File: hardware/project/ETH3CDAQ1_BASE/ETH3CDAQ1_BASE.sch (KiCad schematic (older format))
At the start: 0 parts

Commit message: Schematic design
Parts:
- added H101, H102: MountingHole, MountingHole:MountingHole_2.7mm_M2.5_DIN965_Pad, symbol Mechanical:MountingHole
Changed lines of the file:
@@
 F1 "Channel3.sch" 50
 $EndSheet
+$Comp
+L Mechanical:MountingHole H101
+U 1 1 5FD1DE86
+P 1500 7000
+F 0 "H101" H 1600 7046 50  0000 L CNN
+F 1 "MountingHole" H 1600 6955 50  0000 L CNN
+F 2 "MountingHole:MountingHole_2.7mm_M2.5_DIN965_Pad" H 1500 7000 50  0001 C CNN
+F 3 "~" H 1500 7000 50  0001 C CNN
+	1    1500 7000
+	1    0    0    -1
+$EndComp
+$Comp
+L Mechanical:MountingHole H102
+U 1 1 5FD1EC9A
+P 2350 7000
+F 0 "H102" H 2450 7046 50  0000 L CNN
+F 1 "MountingHole" H 2450 6955 50  0000 L CNN
+F 2 "MountingHole:MountingHole_2.7mm_M2.5_DIN965_Pad" H 2350 7000 50  0001 C CNN
+F 3 "~" H 2350 7000 50  0001 C CNN
+	1    2350 7000
+	1    0    0    -1
+$EndComp
 $EndSCHEMATC

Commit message: PCB layout.
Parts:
- added H103, H104, H105, H106, H107, H108: MountingHole, MountingHole:MountingHole_2.7mm_M2.5_DIN965_Pad, symbol Mechanical:MountingHole
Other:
- moved on the sheet: H101, H102
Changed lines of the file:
@@
 L Mechanical:MountingHole H101
 U 1 1 5FD1DE86
-P 1500 7000
-F 0 "H101" H 1600 7046 50  0000 L CNN
-F 1 "MountingHole" H 1600 6955 50  0000 L CNN
-F 2 "MountingHole:MountingHole_2.7mm_M2.5_DIN965_Pad" H 1500 7000 50  0001 C CNN
-F 3 "~" H 1500 7000 50  0001 C CNN
-	1    1500 7000
+P 900 6700
+F 0 "H101" H 1000 6746 50  0000 L CNN
+F 1 "MountingHole" H 1000 6655 50  0000 L CNN
+F 2 "MountingHole:MountingHole_2.7mm_M2.5_DIN965_Pad" H 900 6700 50  0001 C CNN
+F 3 "~" H 900 6700 50  0001 C CNN
+	1    900  6700
 	1    0    0    -1
 $EndComp
@@
 L Mechanical:MountingHole H102
 U 1 1 5FD1EC9A
-P 2350 7000
-F 0 "H102" H 2450 7046 50  0000 L CNN
-F 1 "MountingHole" H 2450 6955 50  0000 L CNN
-F 2 "MountingHole:MountingHole_2.7mm_M2.5_DIN965_Pad" H 2350 7000 50  0001 C CNN
-F 3 "~" H 2350 7000 50  0001 C CNN
-	1    2350 7000
+P 1750 6700
+F 0 "H102" H 1850 6746 50  0000 L CNN
+F 1 "MountingHole" H 1850 6655 50  0000 L CNN
+F 2 "MountingHole:MountingHole_2.7mm_M2.5_DIN965_Pad" H 1750 6700 50  0001 C CNN
+F 3 "~" H 1750 6700 50  0001 C CNN
+	1    1750 6700
 	1    0    0    -1
 $EndComp
+$Comp
+L Mechanical:MountingHole H105
+U 1 1 5FB9C26E
+P 900 7450
+F 0 "H105" H 1000 7496 50  0000 L CNN
+F 1 "MountingHole" H 1000 7405 50  0000 L CNN
+F 2 "MountingHole:MountingHole_2.7mm_M2.5_DIN965_Pad" H 900 7450 50  0001 C CNN
+F 3 "~" H 900 7450 50  0001 C CNN
+	1    900  7450
+	1    0    0    -1
+$EndComp
+$Comp
+L Mechanical:MountingHole H108
+U 1 1 5FB9C274
+P 1750 7450
+F 0 "H108" H 1850 7496 50  0000 L CNN
+F 1 "MountingHole" H 1850 7405 50  0000 L CNN
+F 2 "MountingHole:MountingHole_2.7mm_M2.5_DIN965_Pad" H 1750 7450 50  0001 C CNN
+F 3 "~" H 1750 7450 50  0001 C CNN
+	1    1750 7450
+	1    0    0    -1
+$EndComp
+$Comp
+L Mechanical:MountingHole H104
+U 1 1 5FB9C81C
+P 900 7200
+F 0 "H104" H 1000 7246 50  0000 L CNN
+F 1 "MountingHole" H 1000 7155 50  0000 L CNN
+F 2 "MountingHole:MountingHole_2.7mm_M2.5_DIN965_Pad" H 900 7200 50  0001 C CNN
+F 3 "~" H 900 7200 50  0001 C CNN
+	1    900  7200
+	1    0    0    -1
+$EndComp
+$Comp
+L Mechanical:MountingHole H107
+U 1 1 5FB9C822
+P 1750 7200
+F 0 "H107" H 1850 7246 50  0000 L CNN
+F 1 "MountingHole" H 1850 7155 50  0000 L CNN
+F 2 "MountingHole:MountingHole_2.7mm_M2.5_DIN965_Pad" H 1750 7200 50  0001 C CNN
+F 3 "~" H 1750 7200 50  0001 C CNN
+	1    1750 7200
+	1    0    0    -1
+$EndComp
+$Comp
+L Mechanical:MountingHole H103
+U 1 1 5FB9CAB2
+P 900 6950
+F 0 "H103" H 1000 6996 50  0000 L CNN
+F 1 "MountingHole" H 1000 6905 50  0000 L CNN
+F 2 "MountingHole:MountingHole_2.7mm_M2.5_DIN965_Pad" H 900 6950 50  0001 C CNN
+F 3 "~" H 900 6950 50  0001 C CNN
+	1    900  6950
+	1    0    0    -1
+$EndComp
+$Comp
+L Mechanical:MountingHole H106
+U 1 1 5FB9CAB8
+P 1750 6950
+F 0 "H106" H 1850 6996 50  0000 L CNN
+F 1 "MountingHole" H 1850 6905 50  0000 L CNN
+F 2 "MountingHole:MountingHole_2.7mm_M2.5_DIN965_Pad" H 1750 6950 50  0001 C CNN
+F 3 "~" H 1750 6950 50  0001 C CNN
+	1    1750 6950
+	1    0    0    -1
+$EndComp

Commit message: PCB design
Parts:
- H101, H102: footprint MountingHole:MountingHole_2.7mm_M2.5_DIN965_Pad -> MountingHole:MountingHole_3.2mm_M3_DIN965_Pad
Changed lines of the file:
@@
 F 0 "H101" H 1000 6746 50  0000 L CNN
 F 1 "MountingHole" H 1000 6655 50  0000 L CNN
-F 2 "MountingHole:MountingHole_2.7mm_M2.5_DIN965_Pad" H 900 6700 50  0001 C CNN
+F 2 "MountingHole:MountingHole_3.2mm_M3_DIN965_Pad" H 900 6700 50  0001 C CNN
 F 3 "~" H 900 6700 50  0001 C CNN
 	1    900  6700
@@
 F 0 "H102" H 1850 6746 50  0000 L CNN
 F 1 "MountingHole" H 1850 6655 50  0000 L CNN
-F 2 "MountingHole:MountingHole_2.7mm_M2.5_DIN965_Pad" H 1750 6700 50  0001 C CNN
+F 2 "MountingHole:MountingHole_3.2mm_M3_DIN965_Pad" H 1750 6700 50  0001 C CNN
 F 3 "~" H 1750 6700 50  0001 C CNN
 	1    1750 6700

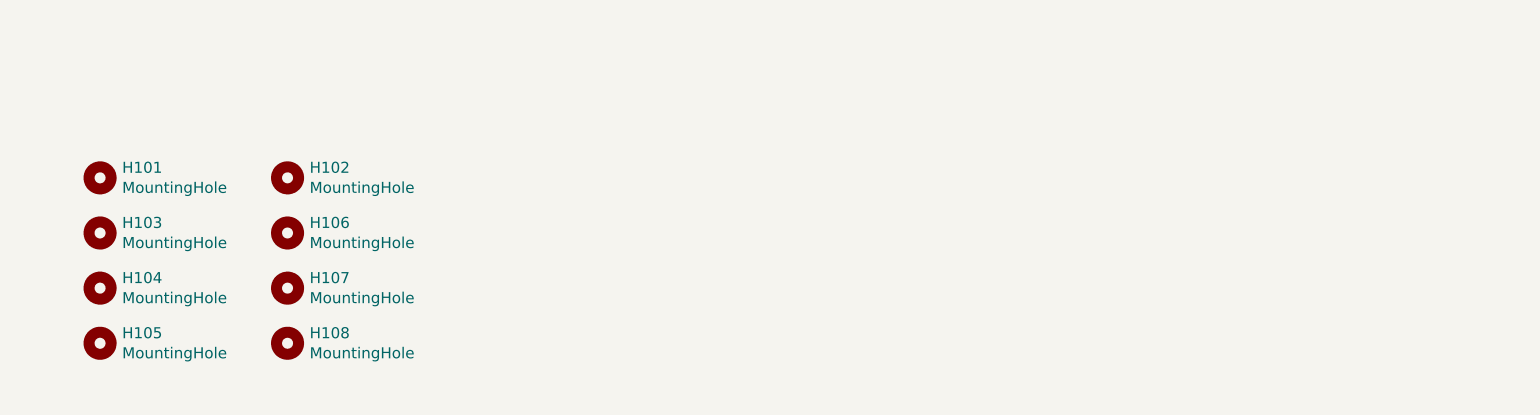
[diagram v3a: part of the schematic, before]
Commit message: Voltage front-end development
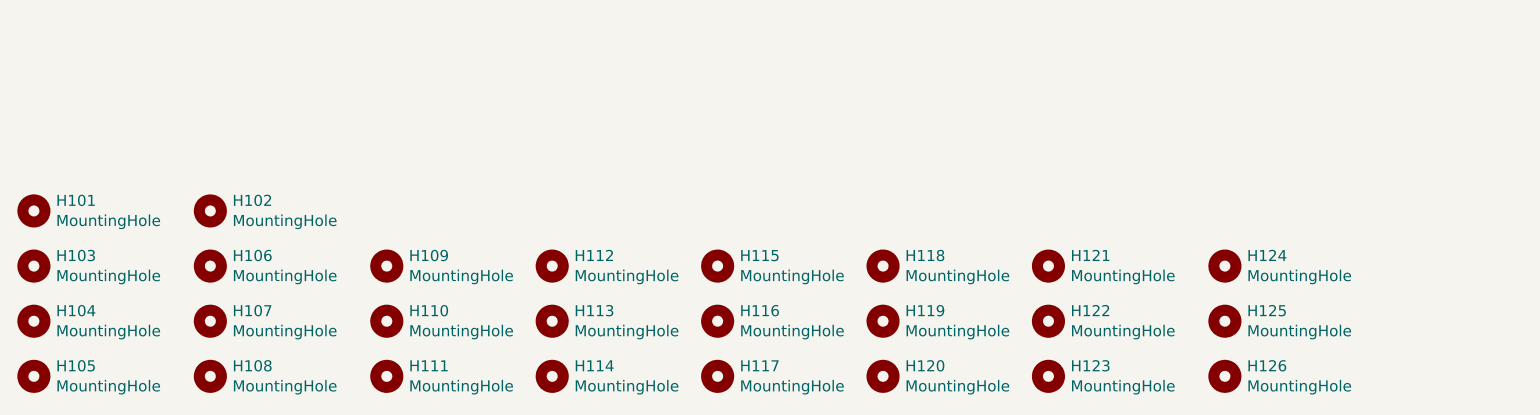
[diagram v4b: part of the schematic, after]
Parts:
- added H109, H110, H111, H112, H113, H114, H115, H116, H117, H118, H119, H120, H121, H122, H123, H124, H125, H126: MountingHole, MountingHole:MountingHole_2.7mm_M2.5_DIN965_Pad, symbol Mechanical:MountingHole
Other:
- moved on the sheet: H101, H102, H103, H104, H105, H106, H107, H108

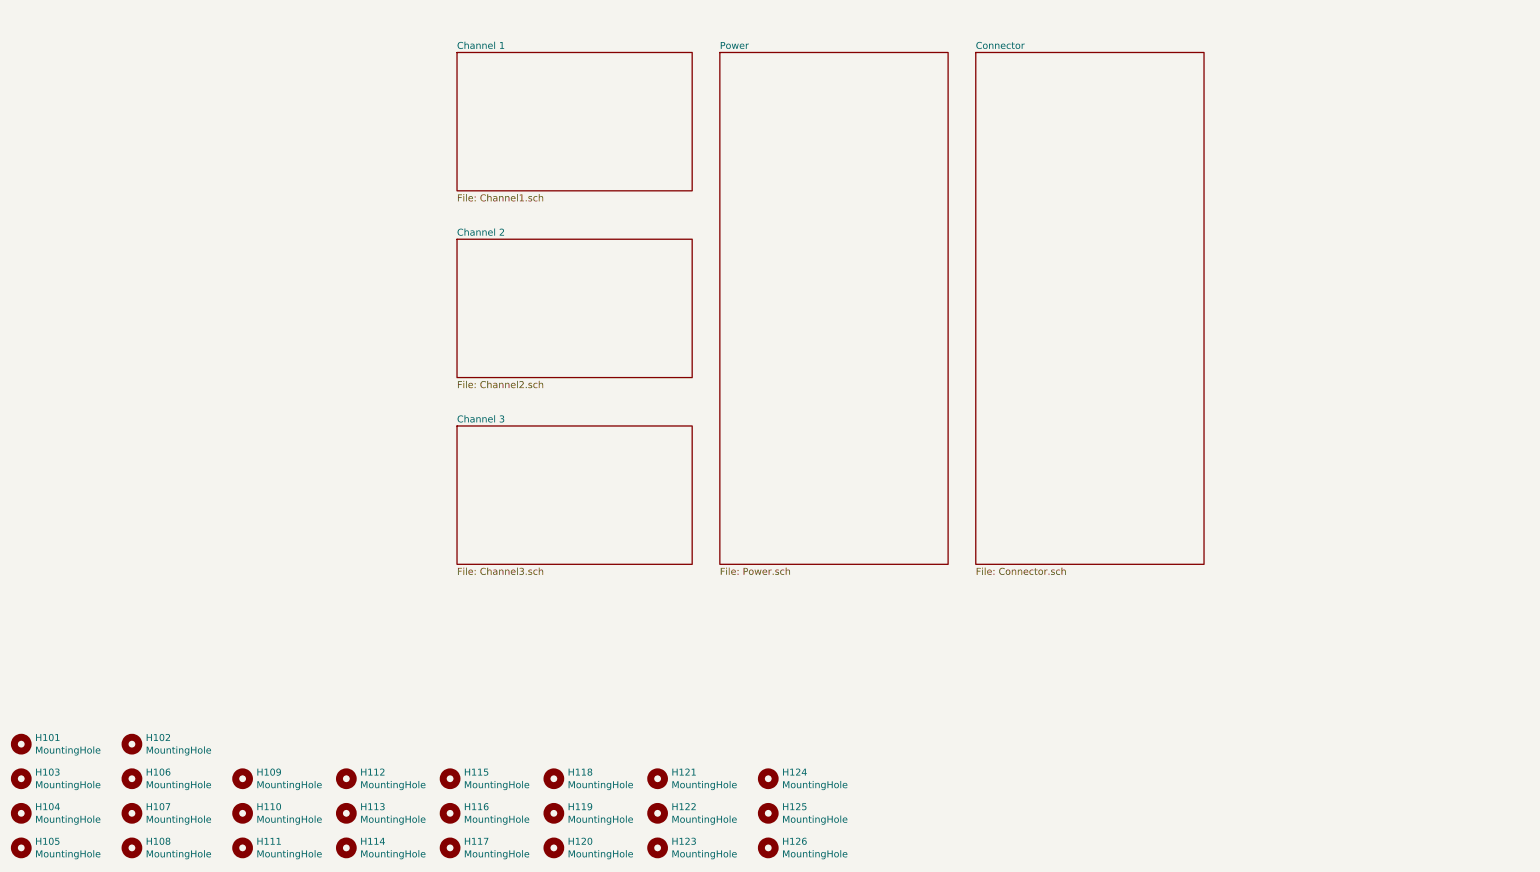
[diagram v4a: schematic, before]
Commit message: Added selftest circuit in the base PCB.
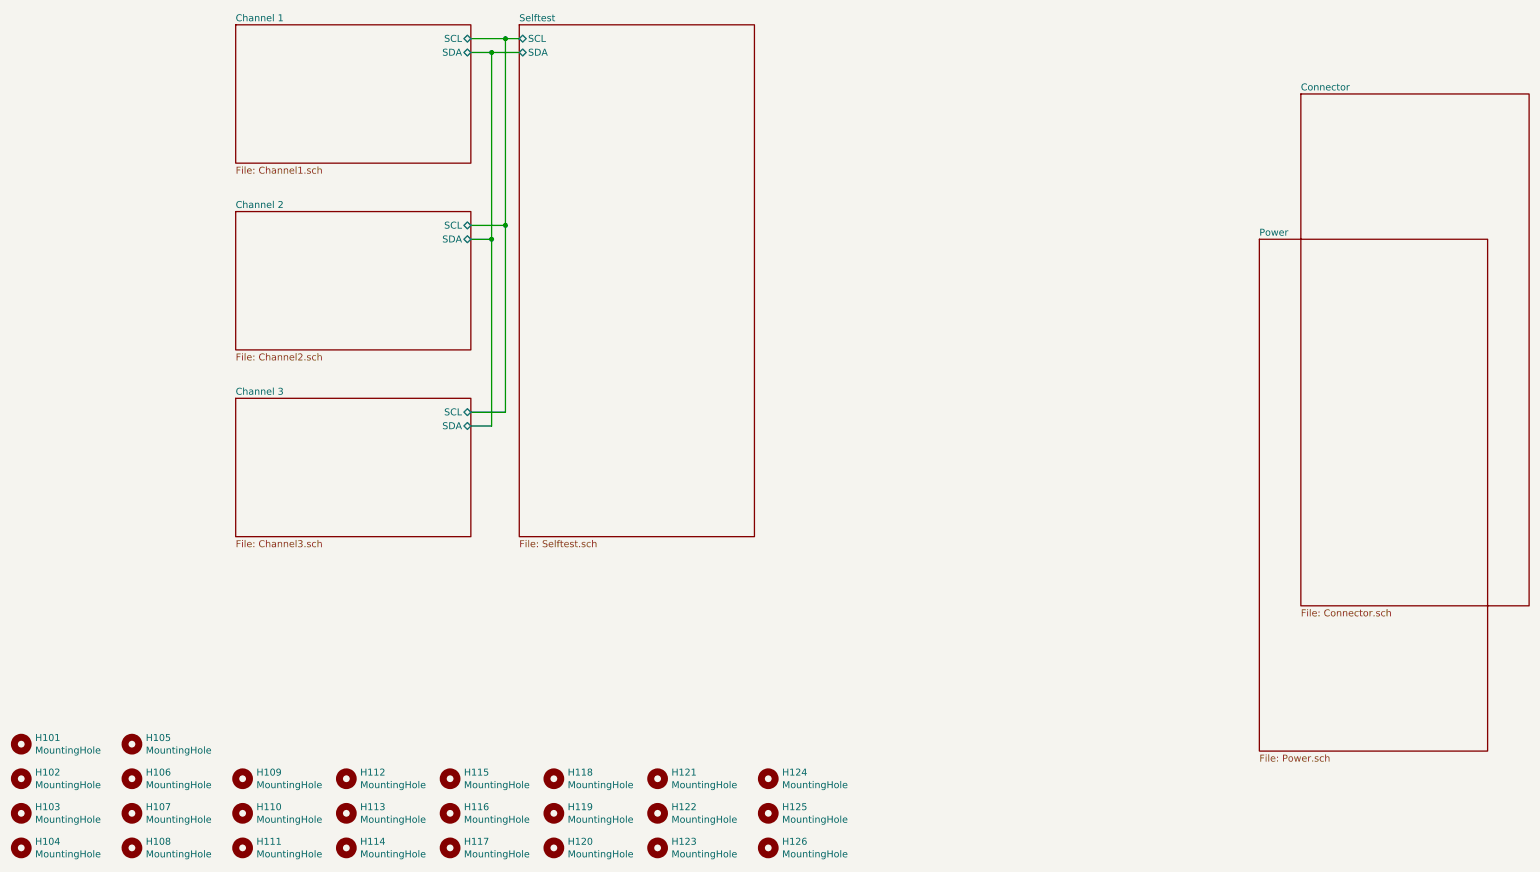
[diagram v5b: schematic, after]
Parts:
- renumbered H103 to H102, H104 to H103, H105 to H104, H102 to H105
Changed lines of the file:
@@
 $Descr A4 11693 8268
 encoding utf-8
-Sheet 1 6
+Sheet 1 7
 Title ""
 Date ""
@@
 $EndDescr
 $Sheet
-S 5650 1850 1650 3700
+S 9550 3200 1650 3700
 U 5FCCA2B9
 F0 "Power" 50
@@
 $EndSheet
 $Sheet
-S 7500 1850 1650 3700
+S 9850 2150 1650 3700
 U 60134E7C
 F0 "Connector" 50
@@
 $EndSheet
 $Sheet
-S 3750 1850 1700 1000
+S 2150 1650 1700 1000
 U 601F1EBA
 F0 "Channel 1" 50
 F1 "Channel1.sch" 50
-$EndSheet
-$Sheet
-S 3750 3200 1700 1000
+F2 "SCL" B R 3850 1750 50
+F3 "SDA" B R 3850 1850 50
+$EndSheet
+$Sheet
+S 2150 3000 1700 1000
 U 602A05D8
 F0 "Channel 2" 50
 F1 "Channel2.sch" 50
-$EndSheet
-$Sheet
-S 3750 4550 1700 1000
+F2 "SCL" B R 3850 3100 50
+F3 "SDA" B R 3850 3200 50
+$EndSheet
+$Sheet
+S 2150 4350 1700 1000
 U 602C0344
 F0 "Channel 3" 50
 F1 "Channel3.sch" 50
+F2 "SCL" B R 3850 4450 50
+F3 "SDA" B R 3850 4550 50
 $EndSheet
 $Comp
@@
 $EndComp
 $Comp
-L Mechanical:MountingHole H102
+L Mechanical:MountingHole H105
 U 1 1 5FD1EC9A
 P 1400 6850
-F 0 "H102" H 1500 6896 50  0000 L CNN
+F 0 "H105" H 1500 6896 50  0000 L CNN
 F 1 "MountingHole" H 1500 6805 50  0000 L CNN
 F 2 "MountingHole:MountingHole_3.2mm_M3_DIN965_Pad" H 1400 6850 50  0001 C CNN
@@
 $EndComp
 $Comp
-L Mechanical:MountingHole H105
+L Mechanical:MountingHole H104
 U 1 1 5FB9C26E
 P 600 7600
-F 0 "H105" H 700 7646 50  0000 L CNN
+F 0 "H104" H 700 7646 50  0000 L CNN
 F 1 "MountingHole" H 700 7555 50  0000 L CNN
 F 2 "MountingHole:MountingHole_2.7mm_M2.5_DIN965_Pad" H 600 7600 50  0001 C CNN
@@
 $EndComp
 $Comp
-L Mechanical:MountingHole H104
+L Mechanical:MountingHole H103
 U 1 1 5FB9C81C
 P 600 7350
-F 0 "H104" H 700 7396 50  0000 L CNN
+F 0 "H103" H 700 7396 50  0000 L CNN
 F 1 "MountingHole" H 700 7305 50  0000 L CNN
 F 2 "MountingHole:MountingHole_2.7mm_M2.5_DIN965_Pad" H 600 7350 50  0001 C CNN
@@
 $EndComp
 $Comp
-L Mechanical:MountingHole H103
+L Mechanical:MountingHole H102
 U 1 1 5FB9CAB2
 P 600 7100
-F 0 "H103" H 700 7146 50  0000 L CNN
+F 0 "H102" H 700 7146 50  0000 L CNN
 F 1 "MountingHole" H 700 7055 50  0000 L CNN
 F 2 "MountingHole:MountingHole_2.7mm_M2.5_DIN965_Pad" H 600 7100 50  0001 C CNN
@@
 	1    0    0    -1
 $EndComp
+$Sheet
+S 4200 1650 1700 3700
+U 5FCCC26E
+F0 "Selftest" 50
+F1 "Selftest.sch" 50
+F2 "SCL" B L 4200 1750 50
+F3 "SDA" B L 4200 1850 50
+$EndSheet
+Wire Wire Line
+	4200 1850 4000 1850
+Wire Wire Line
+	3850 1750 4100 1750
+Wire Wire Line
+	4100 1750 4100 3100
+Wire Wire Line
+	4100 4450 3850 4450
+Connection ~ 4100 1750
+Wire Wire Line
+	4100 1750 4200 1750
+Wire Wire Line
+	3850 3100 4100 3100
+Connection ~ 4100 3100
+Wire Wire Line
+	4100 3100 4100 4450
+Wire Wire Line
+	3850 4550 4000 4550
+Wire Wire Line
+	4000 4550 4000 3200
+Connection ~ 4000 1850
+Wire Wire Line
+	4000 1850 3850 1850
+Wire Wire Line
+	3850 3200 4000 3200
+Connection ~ 4000 3200
+Wire Wire Line
+	4000 3200 4000 1850
 $EndSCHEMATC

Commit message: Modifications in PCB and schematic in the base module.
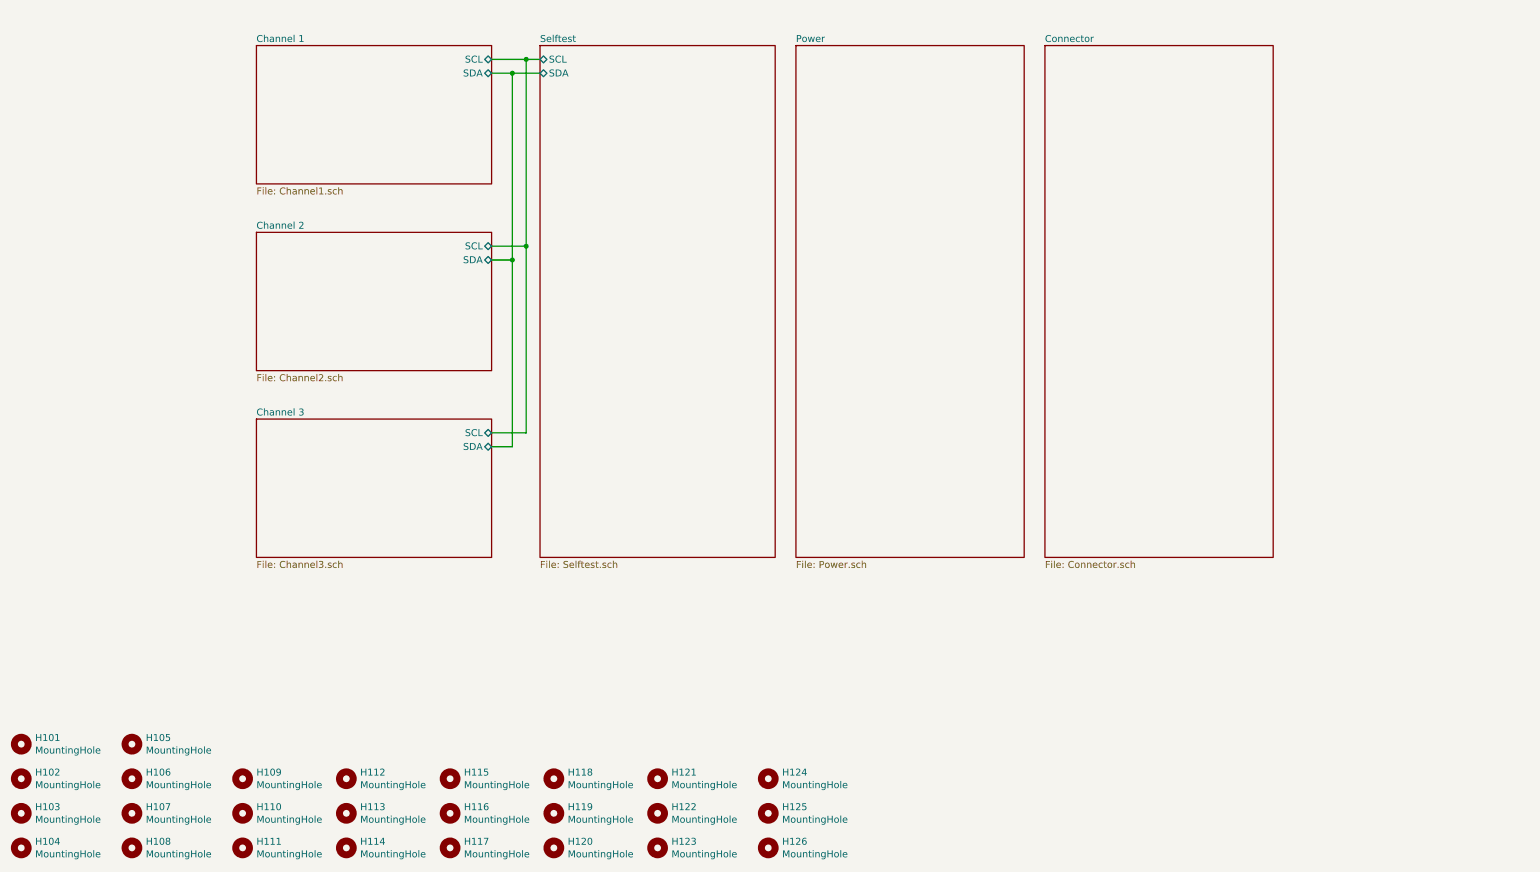
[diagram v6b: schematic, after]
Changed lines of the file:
@@
 $EndDescr
 $Sheet
-S 9550 3200 1650 3700
+S 6200 1800 1650 3700
 U 5FCCA2B9
 F0 "Power" 50
@@
 $EndSheet
 $Sheet
-S 9850 2150 1650 3700
+S 8000 1800 1650 3700
 U 60134E7C
 F0 "Connector" 50
@@
 $EndSheet
 $Sheet
-S 2150 1650 1700 1000
+S 2300 1800 1700 1000
 U 601F1EBA
 F0 "Channel 1" 50
 F1 "Channel1.sch" 50
-F2 "SCL" B R 3850 1750 50
-F3 "SDA" B R 3850 1850 50
-$EndSheet
-$Sheet
-S 2150 3000 1700 1000
+F2 "SCL" B R 4000 1900 50
+F3 "SDA" B R 4000 2000 50
+$EndSheet
+$Sheet
+S 2300 3150 1700 1000
 U 602A05D8
 F0 "Channel 2" 50
 F1 "Channel2.sch" 50
-F2 "SCL" B R 3850 3100 50
-F3 "SDA" B R 3850 3200 50
-$EndSheet
-$Sheet
-S 2150 4350 1700 1000
+F2 "SCL" B R 4000 3250 50
+F3 "SDA" B R 4000 3350 50
+$EndSheet
+$Sheet
+S 2300 4500 1700 1000
 U 602C0344
 F0 "Channel 3" 50
 F1 "Channel3.sch" 50
-F2 "SCL" B R 3850 4450 50
-F3 "SDA" B R 3850 4550 50
+F2 "SCL" B R 4000 4600 50
+F3 "SDA" B R 4000 4700 50
 $EndSheet
 $Comp
@@
 $EndComp
 $Sheet
-S 4200 1650 1700 3700
+S 4350 1800 1700 3700
 U 5FCCC26E
 F0 "Selftest" 50
 F1 "Selftest.sch" 50
-F2 "SCL" B L 4200 1750 50
-F3 "SDA" B L 4200 1850 50
-$EndSheet
-Wire Wire Line
-	4200 1850 4000 1850
-Wire Wire Line
-	3850 1750 4100 1750
-Wire Wire Line
-	4100 1750 4100 3100
-Wire Wire Line
-	4100 4450 3850 4450
-Connection ~ 4100 1750
-Wire Wire Line
-	4100 1750 4200 1750
-Wire Wire Line
-	3850 3100 4100 3100
-Connection ~ 4100 3100
-Wire Wire Line
-	4100 3100 4100 4450
-Wire Wire Line
-	3850 4550 4000 4550
-Wire Wire Line
-	4000 4550 4000 3200
-Connection ~ 4000 1850
-Wire Wire Line
-	4000 1850 3850 1850
-Wire Wire Line
-	3850 3200 4000 3200
-Connection ~ 4000 3200
-Wire Wire Line
-	4000 3200 4000 1850
+F2 "SCL" B L 4350 1900 50
+F3 "SDA" B L 4350 2000 50
+$EndSheet
+Wire Wire Line
+	4350 2000 4150 2000
+Wire Wire Line
+	4000 1900 4250 1900
+Wire Wire Line
+	4250 1900 4250 3250
+Wire Wire Line
+	4250 4600 4000 4600
+Connection ~ 4250 1900
+Wire Wire Line
+	4250 1900 4350 1900
+Wire Wire Line
+	4000 3250 4250 3250
+Connection ~ 4250 3250
+Wire Wire Line
+	4250 3250 4250 4600
+Wire Wire Line
+	4000 4700 4150 4700
+Wire Wire Line
+	4150 4700 4150 3350
+Connection ~ 4150 2000
+Wire Wire Line
+	4150 2000 4000 2000
+Wire Wire Line
+	4000 3350 4150 3350
+Connection ~ 4150 3350
+Wire Wire Line
+	4150 3350 4150 2000
 $EndSCHEMATC
